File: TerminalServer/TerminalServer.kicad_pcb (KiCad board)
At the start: 4 copper layers, 135 x 72 mm, 129 parts, among them J1 RJ45_LED, J10 Conn_01x10_Pin, J11 SI-60118-F, J12 Conn_01x08_Pin, J13 503398-1892, J2 RJ45_LED, J3 RJ45_LED, J4 RJ45_LED, J5 RJ45_LED, J6 RJ45_LED, J7 USB_B, J8 Barrel_Jack_Switch, J9 Conn_PIC_ICSP_ICD, SW1 SW_Push, SW2 SW_SPDT, U1 PIC32MX795F512L-80x-PT, U10 24LC16, U11 ENC28J60x-ML, U12 ESP32-S3-WROOM-1, U2 XR32330EBERTR-F, U3 XR32330EBERTR-F, U4 XR32330EBERTR-F, U5 XR32330EBERTR-F, U6 XR32330EBERTR-F, U7 XR32330EBERTR-F, U9 TPS82130, Y1 ASEMB-8.000MHZ-LC-T, Y2 ASEMB-25.000MHZ-LC-T

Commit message: Initial firmware work
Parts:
- added R35: 10k, Resistor_SMD:R_0603_1608Metric_Pad0.98x0.95mm_HandSolder, F.Cu at (90.8, 92.0)
- added R36: 10k, Resistor_SMD:R_0603_1608Metric_Pad0.98x0.95mm_HandSolder, F.Cu at (122.7, 91.9)
- SW2: footprint Button_Switch_THT:SW_Slide_SP3T_Straight_CK_OS103012MU1QP1 -> Library:34ASP23B4M7RT
- moved SW2 3.70 mm to (190.8, 66.4)
- moved C52 1.70 mm to (198.6, 87.5)
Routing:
- net VDD: track 160.3 -> 162.9 mm, vias 42 -> 44
- net /ENC_INT: track 62.8 -> 65.0 mm
- net /ESP_INT: track 74.0 -> 75.1 mm
- net /SWIN: track 12.9 -> 12.2 mm

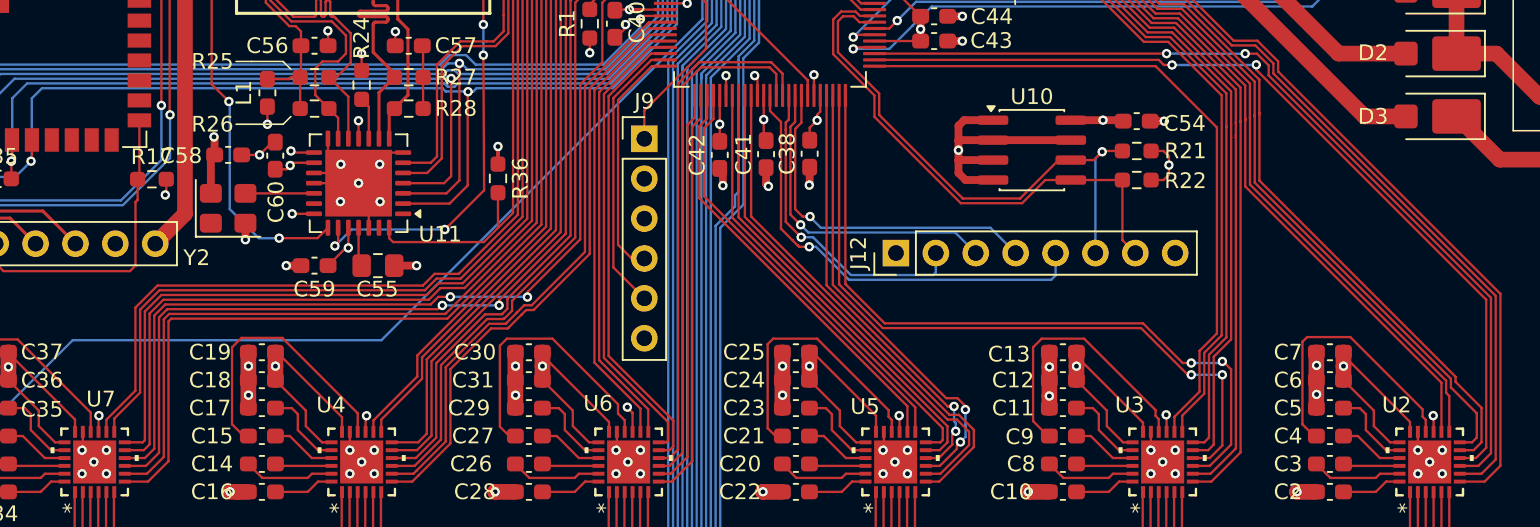
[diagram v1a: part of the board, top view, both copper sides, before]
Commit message: Tie A2 of EEPROM high and move RS232 driver SHUTDOWN (now tied high) to ONLINE pin.
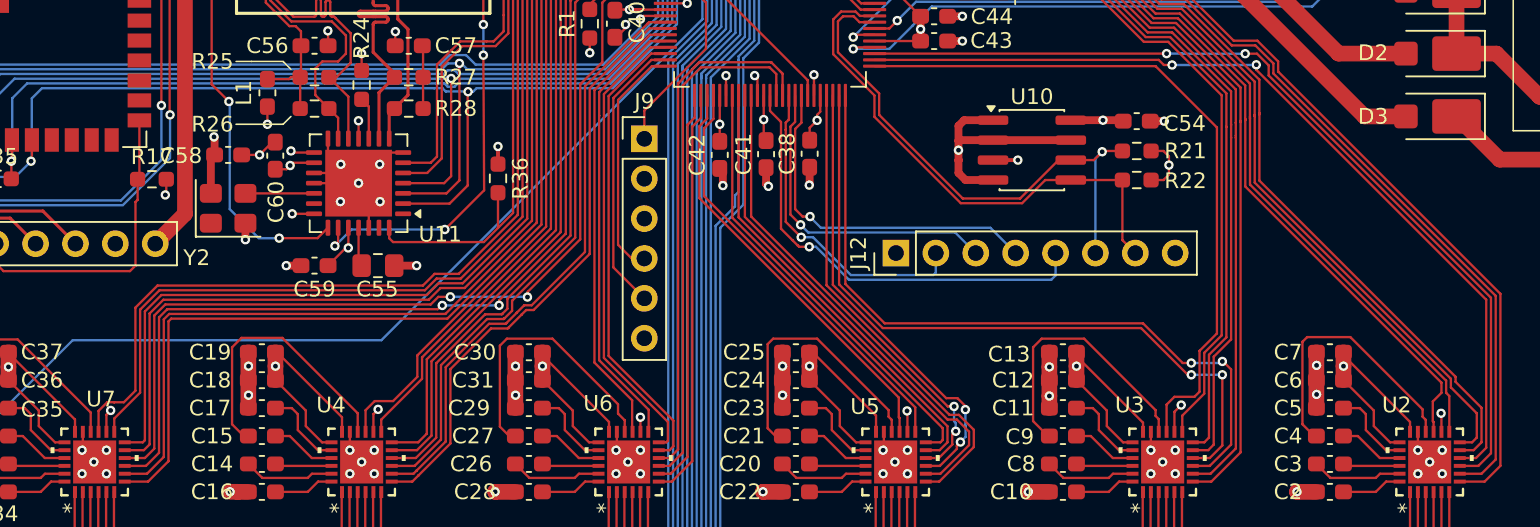
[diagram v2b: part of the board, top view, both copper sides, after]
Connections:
- U10 pad 3: GND -> VDD
- U2 pad 14: /U1SHTDN -> VDD
- U2 pad 15: VDD -> /U1SHTDN
- U3 pad 14: /U2SHTDN -> VDD
- U3 pad 15: VDD -> /U2SHTDN
- U4 pad 14: /U3SHTDN -> VDD
- U4 pad 15: VDD -> /U3SHTDN
- U5 pad 14: /U4SHTDN -> VDD
- U5 pad 15: VDD -> /U4SHTDN
- U6 pad 14: /U5SHTDN -> VDD
- U6 pad 15: VDD -> /U5SHTDN
- U7 pad 14: /U6SHTDN -> VDD
- U7 pad 15: VDD -> /U6SHTDN
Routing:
- net VDD: track 162.9 -> 165.9 mm, vias 44 -> 45
- net GND: track 118.7 -> 116.5 mm
- net /U2SHTDN: track 43.9 -> 44.9 mm
- net /U3SHTDN: track 41.5 -> 42.4 mm
- net /U6SHTDN: track 69.6 -> 70.5 mm
